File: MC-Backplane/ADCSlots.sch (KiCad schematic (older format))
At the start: 0 parts

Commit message: added reverse polarity protection circuit and fuse
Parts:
- added U? (x4): 86094328314755V1LF, symbol MC-Backplane:86094328314755V1LF
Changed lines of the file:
@@
 $Descr A4 11693 8268
 encoding utf-8
-Sheet 1 5
+Sheet 4 5
 Title ""
 Date ""
@@
 Comment4 ""
 $EndDescr
+$Comp
+L MC-Backplane:86094328314755V1LF U?
+U 1 1 61F36CAB
+P 2400 3200
+F 0 "U?" H 2400 5017 50  0000 C CNN
+F 1 "86094328314755V1LF" H 2400 4926 50  0000 C CNN
+F 2 "" H 2400 3200 50  0001 C CNN
+F 3 "" H 2400 3200 50  0001 C CNN
+	1    2400 3200
+	1    0    0    -1
+$EndComp
+$Comp
+L MC-Backplane:86094328314755V1LF U?
+U 1 1 61F38956
+P 4600 5800
+F 0 "U?" H 4600 7617 50  0000 C CNN
+F 1 "86094328314755V1LF" H 4600 7526 50  0000 C CNN
+F 2 "" H 4600 5800 50  0001 C CNN
+F 3 "" H 4600 5800 50  0001 C CNN
+	1    4600 5800
+	1    0    0    -1
+$EndComp
+$Comp
+L MC-Backplane:86094328314755V1LF U?
+U 1 1 61F3C445
+P 6750 3250
+F 0 "U?" H 6750 5067 50  0000 C CNN
+F 1 "86094328314755V1LF" H 6750 4976 50  0000 C CNN
+F 2 "" H 6750 3250 50  0001 C CNN
+F 3 "" H 6750 3250 50  0001 C CNN
+	1    6750 3250
+	1    0    0    -1
+$EndComp
+$Comp
+L MC-Backplane:86094328314755V1LF U?
+U 1 1 61F3F958
+P 9350 5750
+F 0 "U?" H 9350 7567 50  0000 C CNN
+F 1 "86094328314755V1LF" H 9350 7476 50  0000 C CNN
+F 2 "" H 9350 5750 50  0001 C CNN
+F 3 "" H 9350 5750 50  0001 C CNN
+	1    9350 5750
+	1    0    0    -1
+$EndComp
 $EndSCHEMATC

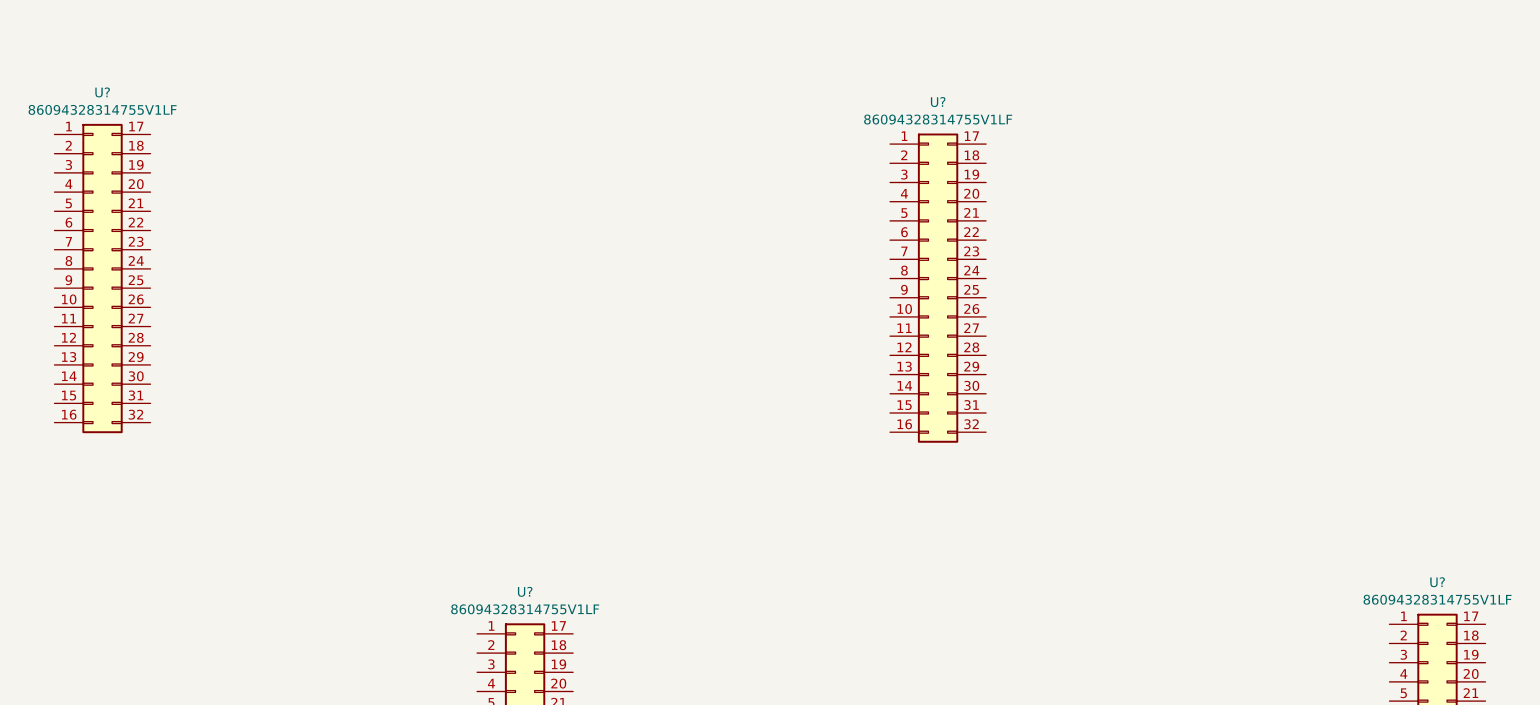
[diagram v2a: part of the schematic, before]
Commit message: added signals for FO slots
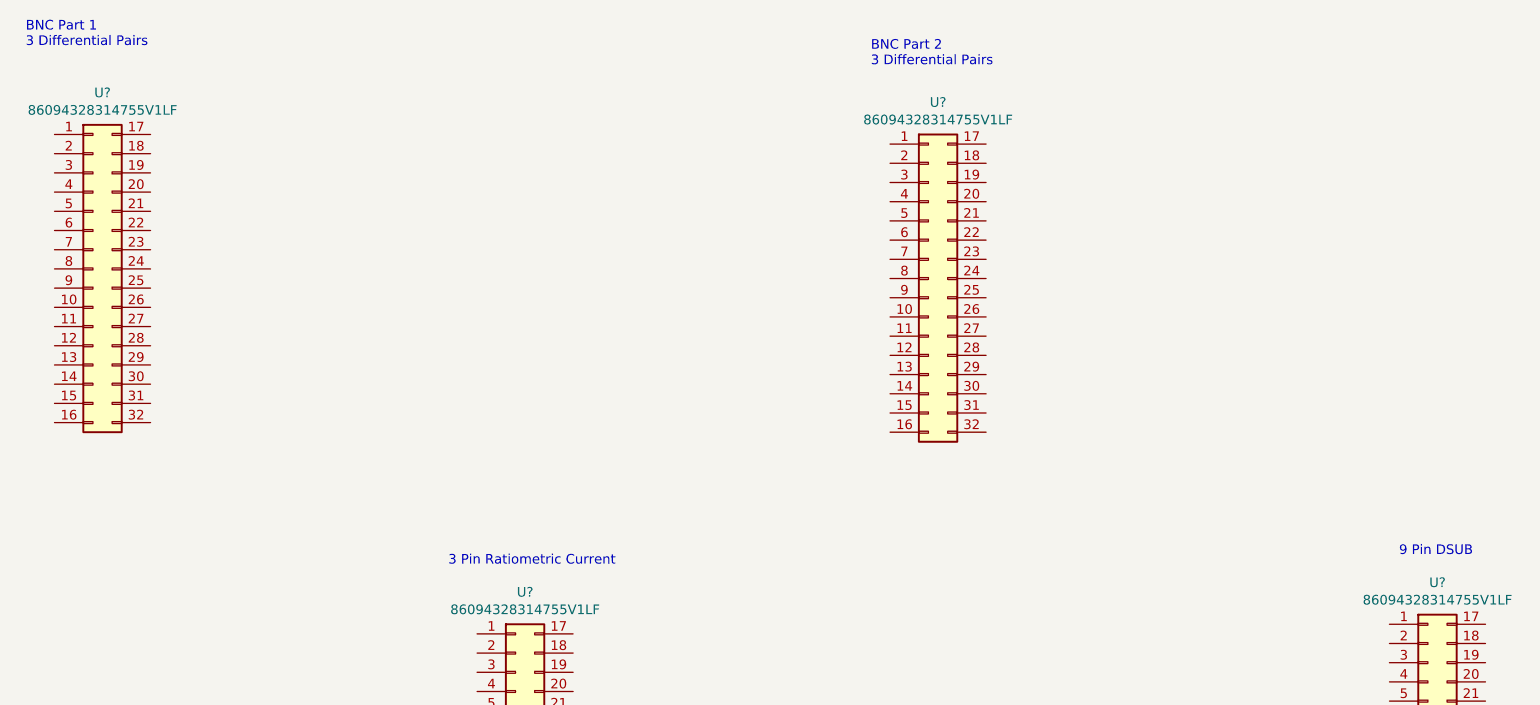
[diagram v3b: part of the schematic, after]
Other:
- note added: "9 Pin DSUB"
- note added: "BNC Part 1\n3 Differential Pairs"
- note added: "BNC Part 2\n3 Differential Pairs"
- note added: "\n3 Pin Ratiometric Current"
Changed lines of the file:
@@
 $Descr A4 11693 8268
 encoding utf-8
-Sheet 4 6
+Sheet 3 7
 Title ""
 Date ""
@@
 	1    0    0    -1
 $EndComp
+Text Notes 2000 1150 0    50   ~ 0
+BNC Part 1\n3 Differential Pairs
+Text Notes 6400 1250 0    50   ~ 0
+BNC Part 2\n3 Differential Pairs
+Text Notes 4200 3850 0    50   ~ 0
+\n3 Pin Ratiometric Current
+Text Notes 9150 3800 0    50   ~ 0
+9 Pin DSUB
 $EndSCHEMATC

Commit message: Add files via upload
updating net names and wires
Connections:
- net labels added: 24V, ADCIN14, ADCIN15, ADCINA2, ADCINA3, ADCINA4, ADCINA5, ADCINB2, ADCINB3, ADCINC2, ADCINC3, ADCINC4, ADCINC5, GND, SAFE_STATE_FLAG
- wire segments 0 -> 226
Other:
- note added: "BNC Part 1\n"
- note added: "BNC Part 2\n"
- note added: "The BNC card / 3-wire current card only use single-\nended so it's hard to say right now. I think at this point\n"
- note removed: "BNC Part 1\n3 Differential Pairs"
- note removed: "BNC Part 2\n3 Differential Pairs"

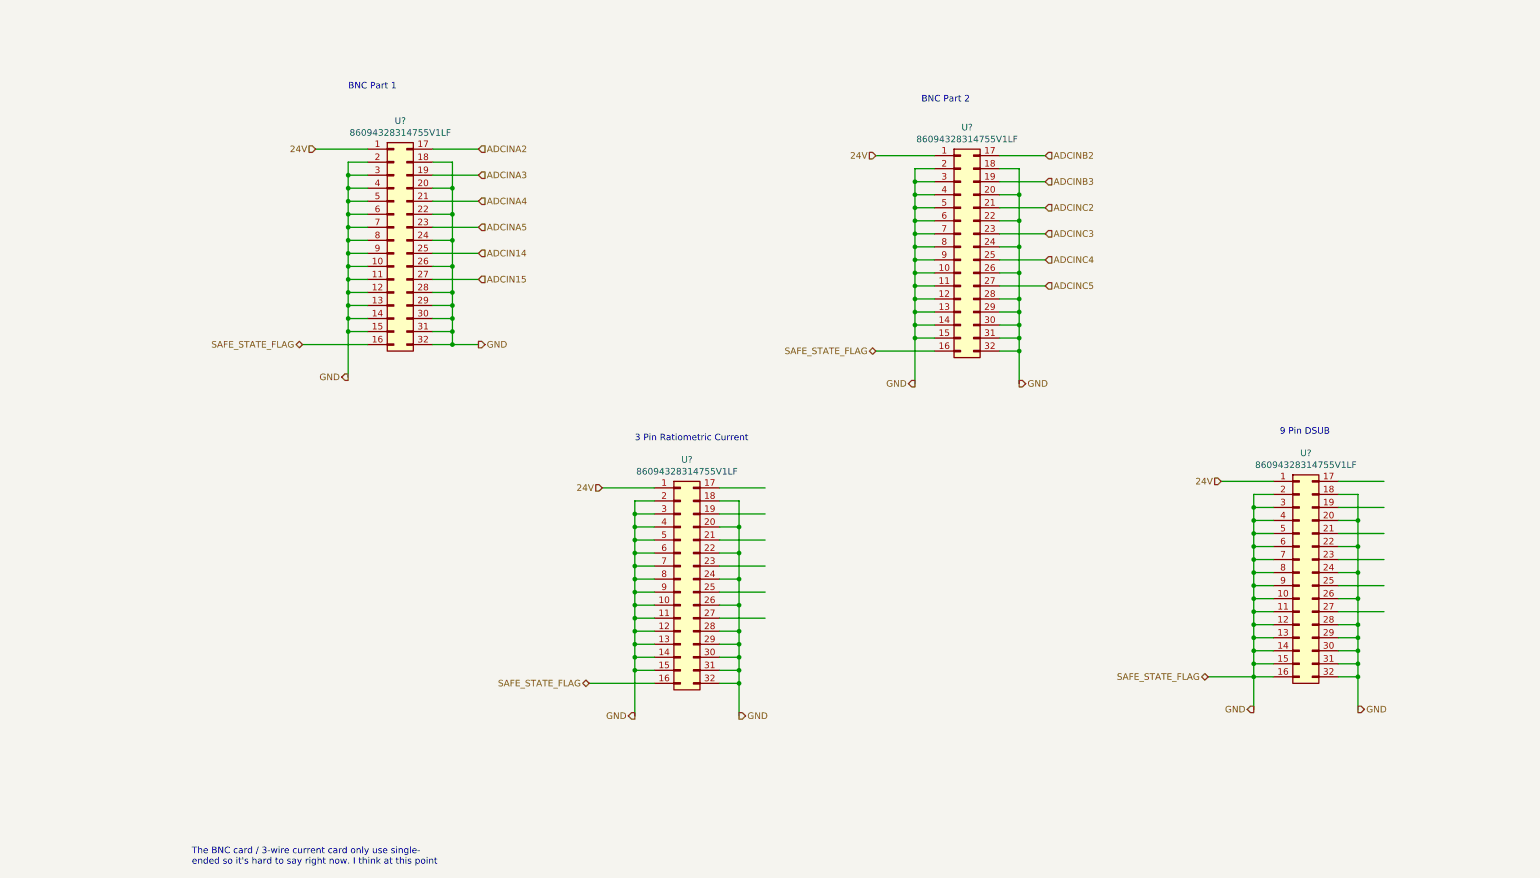
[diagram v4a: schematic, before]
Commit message: Signal naming cleanup/ dsp pin pairing
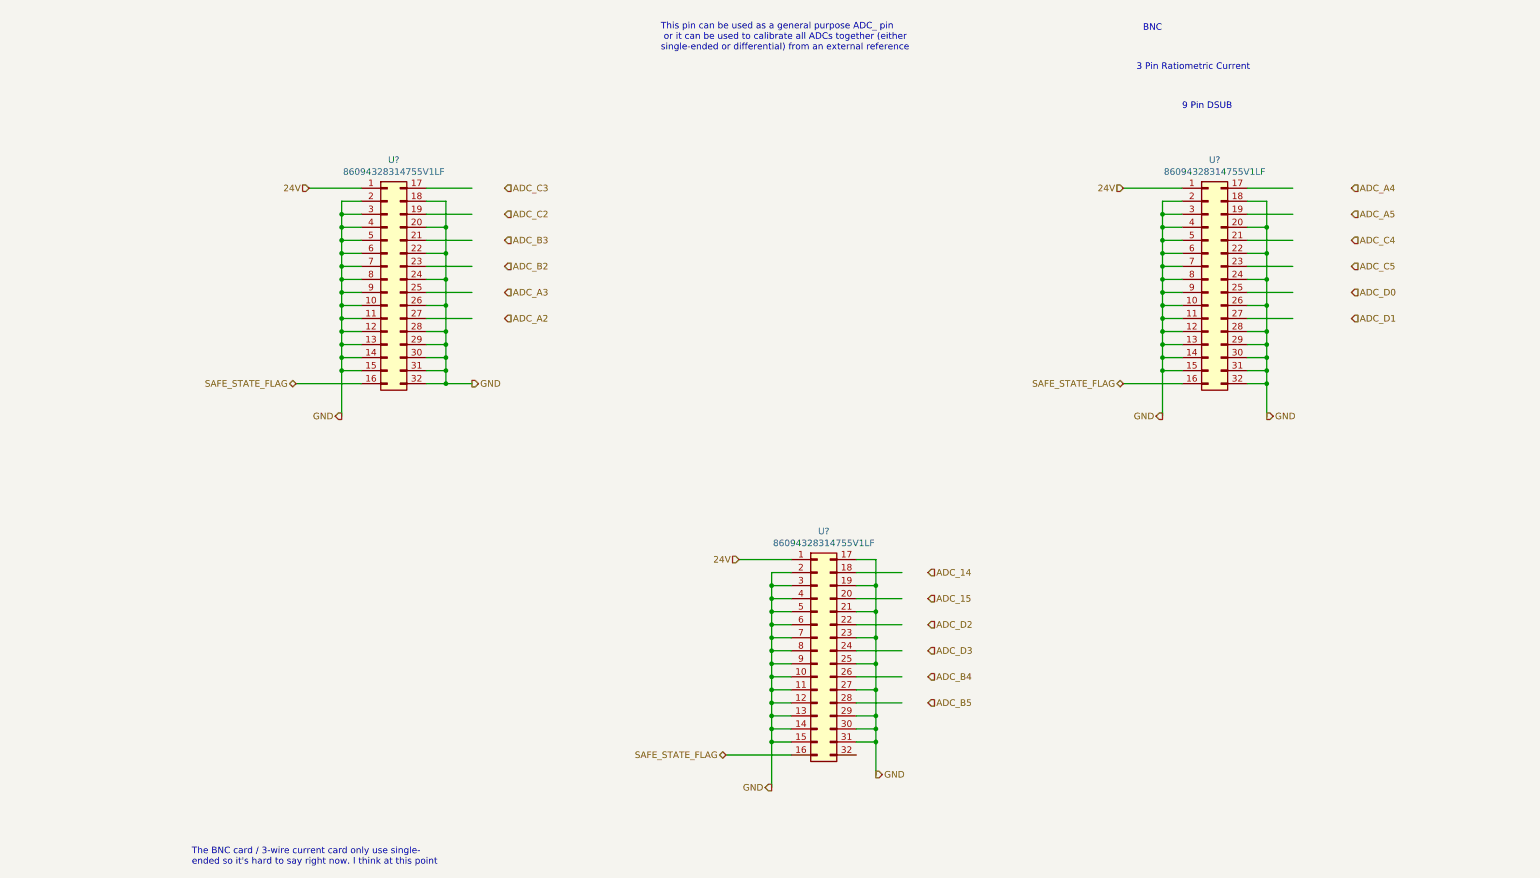
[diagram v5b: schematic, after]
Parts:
- removed U?: 86094328314755V1LF, symbol MC-Backplane:86094328314755V1LF
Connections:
- net labels added: ADC_14, ADC_15, ADC_A2, ADC_A3, ADC_A4, ADC_A5, ADC_B2, ADC_B3, ADC_B4, ADC_B5, ADC_C2, ADC_C3, ADC_C4, ADC_C5, ADC_D0, ADC_D1, ADC_D2, ADC_D3
- net labels removed: ADCIN14, ADCIN15, ADCINA2, ADCINA3, ADCINA4, ADCINA5, ADCINB2, ADCINB3, ADCINC2, ADCINC3, ADCINC4, ADCINC5
- wire segments 226 -> 166
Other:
- note added: "BNC"
- note added: "This pin can be used as a general purpose ADC_ pin\n or it can be used to calibrate all ADCs together (either \nsingle-ended or differential) from an external reference"
- note removed: "BNC Part 1\n"
- note removed: "BNC Part 2\n"
- moved on the sheet: U?

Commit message: DSP interface pin out
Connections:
- net labels added: CLOCK, ~GPIO13_SAFE_STATE_FLAG~
- net labels removed: SAFE_STATE_FLAG
- wire segments 166 -> 168
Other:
- note added: "SLOT 10"
- note added: "SLOT 11"
- note added: "SLOT 12"
- moved on the sheet: U?

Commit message: beginning layout
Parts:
- removed U? (x3): 86094328314755V1LF, symbol MC-Backplane:86094328314755V1LF
- added J41, J42, J43: 86094328314755V1LF, 86094328314755V1LF, symbol Existing_IC_Models:86094328314755V1LF
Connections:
- net 24V: now also J41.A1, J41.A2, J42.A1, J42.A2, J43.A1, J43.A2
- net ADC_14: now also J43.A8
- net ADC_15: now also J43.A10
- net ADC_A2: now also J41.A8
- net ADC_A3: now also J41.A10
- net ADC_A4: now also J42.A8
- net ADC_A5: now also J42.A10
- net ADC_B2: now also J41.A12
- net ADC_B3: now also J41.C11
- net ADC_B4: now also J43.A12
- net ADC_B5: now also J43.C11
- net ADC_C2: now also J41.C13
- net ADC_C3: now also J41.C15
- net ADC_C4: now also J42.A12
- net ADC_C5: now also J42.C11
- net ADC_D0: now also J42.C13
- net ADC_D1: now also J42.C15
- net ADC_D2: now also J43.C13
- net ADC_D3: now also J43.C15
- net CLOCK: now also J41.C4, J42.C4, J43.C4
- net GND: now also J41.A11, J41.A13, J41.A14, J41.A15, J41.A3, J41.A4, J41.A5, J41.A6, J41.A7, J41.A9, J41.B1, J41.B10, J41.B11, J41.B12, J41.B13, J41.B14, J41.B15, J41.B16, J41.B2, J41.B3, J41.B4, J41.B5, J41.B6, J41.B7, J41.B8, J41.B9, J41.C1, J41.C10, J41.C12, J41.C14, J41.C16, J41.C2, J41.C3, J41.C5, J41.C6, J41.C7, J41.C8, J41.C9, J42.A11, J42.A13, J42.A14, J42.A15, J42.A3, J42.A4, J42.A5, J42.A6, J42.A7, J42.A9, J42.B1, J42.B10, J42.B11, J42.B12, J42.B13, J42.B14, J42.B15, J42.B16, J42.B2, J42.B3, J42.B4, J42.B5, J42.B6, J42.B7, J42.B8, J42.B9, J42.C1, J42.C10, J42.C12, J42.C14, J42.C16, J42.C2, J42.C3, J42.C5, J42.C6, J42.C7, J42.C8, J42.C9, J43.A11, J43.A13, J43.A14, J43.A15, J43.A3, J43.A4, J43.A5, J43.A6, J43.A7, J43.A9, J43.B1, J43.B2, J43.B3, J43.B4, J43.B5, J43.B6, J43.B7, J43.B8, J43.B9
- net ~GPIO13_SAFE_STATE_FLAG~: now also J41.A16, J42.A16, J43.A16
- new net: J43.B10, J43.B11, J43.B12, J43.B13, J43.B14, J43.B15, J43.B16, J43.C1, J43.C10, J43.C12, J43.C14, J43.C16, J43.C2, J43.C3, J43.C5, J43.C6, J43.C7, J43.C8, J43.C9
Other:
- note removed: "The BNC card / 3-wire current card only use single-\nended so it's hard to say right now. I think at this point\n"
- note removed: "This pin can be used as a general purpose ADC_ pin\n or it can be used to calibrate all ADCs together (either \nsingle-ended or differential) from an external reference"
